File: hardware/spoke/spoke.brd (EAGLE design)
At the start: 53.3 x 37.8 mm, 22 parts, among them IC1 7805, J1 AVR_SPI_PRG_6PTH, J2 POWER_JACKPTH, U1 ATMEGA328P_PDIP, U2 AT25M01-SHM-B, U3 NRF24L01+

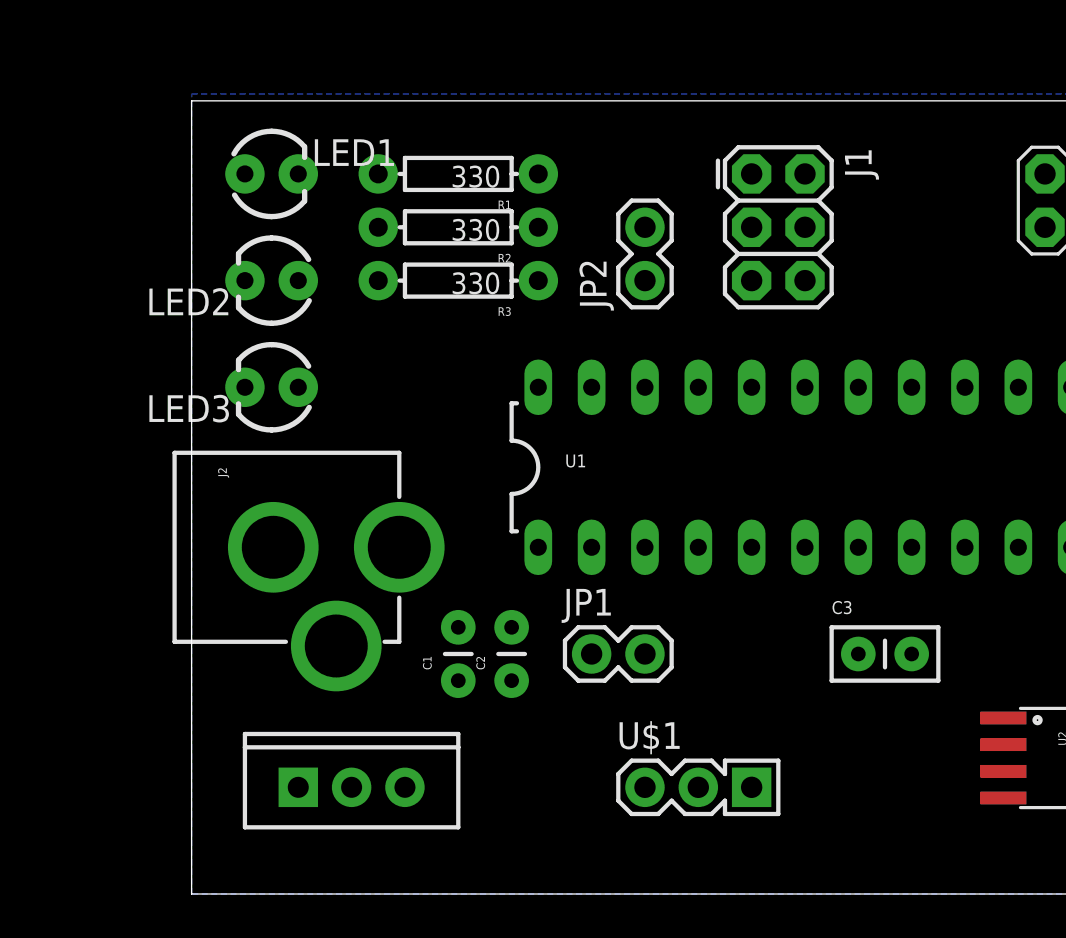
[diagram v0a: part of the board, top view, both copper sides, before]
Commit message: MOAR SMDs and 3.3v supply fixes
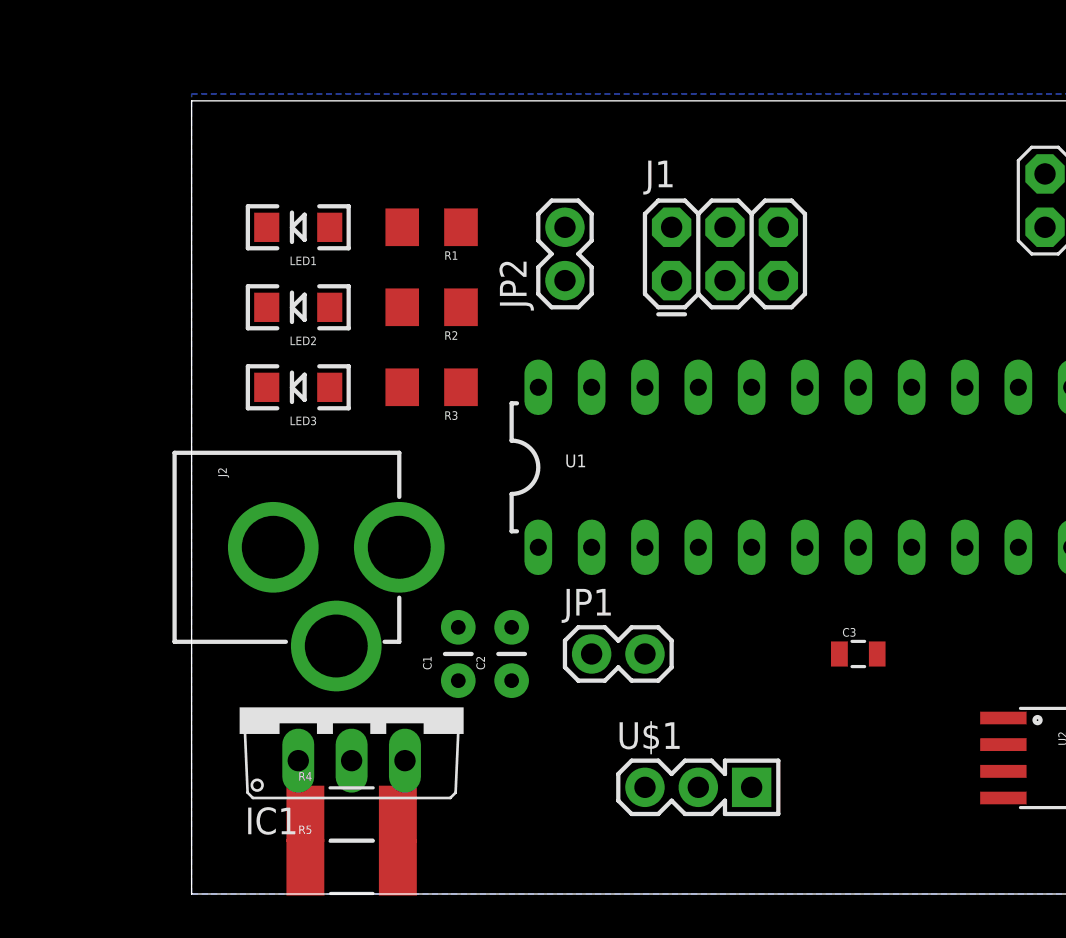
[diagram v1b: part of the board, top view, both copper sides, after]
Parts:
- added R4: 50, SparkFun-Passives:R2010
- added R5: 100, SparkFun-Passives:R2010
- C3: device SparkFun-Capacitors:CAP-PTH-SMALLEZ -> SparkFun-Passives:0805
- IC1: value 7805 -> 7805TV; device SparkFun-PowerIC:TO220-IGO -> linear:TO220V
- LED1, LED2, LED3: device SparkFun-LED:LED3MM -> SparkFun-LED:LED-1206
- R1, R2, R3: device SparkFun-Passives:AXIAL-0.3EZ -> SparkFun-Passives:1206
- moved J1 6.35 mm to (22.9, 29.2), turned to 0 degrees
- moved R3 5.24 mm to (11.4, 24.1)
- moved R2 4.02 mm to (11.4, 27.9)
- moved IC1 3.81 mm to (7.62, 8.89)
- moved JP2 3.81 mm to (17.8, 29.2)
- moved LED1 2.84 mm to (5.08, 31.8), turned to 180 degrees
- moved R1 2.84 mm to (11.4, 31.8)
- moved LED2 1.80 mm to (5.08, 27.9)
- moved LED3 1.27 mm to (5.08, 24.1)
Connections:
- removed net VCC: C2.1, C3.1, IC1.OUT, J1.2, U$1.1, U1.7, U2.8, U3.2
- new net 3.3V: R4.2, R5.1, U2.8
- new net 5V: C2.1, C3.1, IC1.3, J1.2, R4.1, U$1.1, U1.7, U3.2
- net GND: now also IC1.2, LED1.C, LED2.C, LED3.C, R5.2; no longer IC1.GND, LED1.K, LED2.K, LED3.K
- net N$10: now also R1.2; no longer R1.P$2
- net N$11: now also R3.2; no longer R3.P$2
- net N$12: now also R1.1; no longer R1.P$1
- net N$13: now also R3.1; no longer R3.P$1
- net N$14: now also IC1.1; no longer IC1.IN
- net N$8: now also R2.2; no longer R2.P$2
- net N$9: now also R2.1; no longer R2.P$1

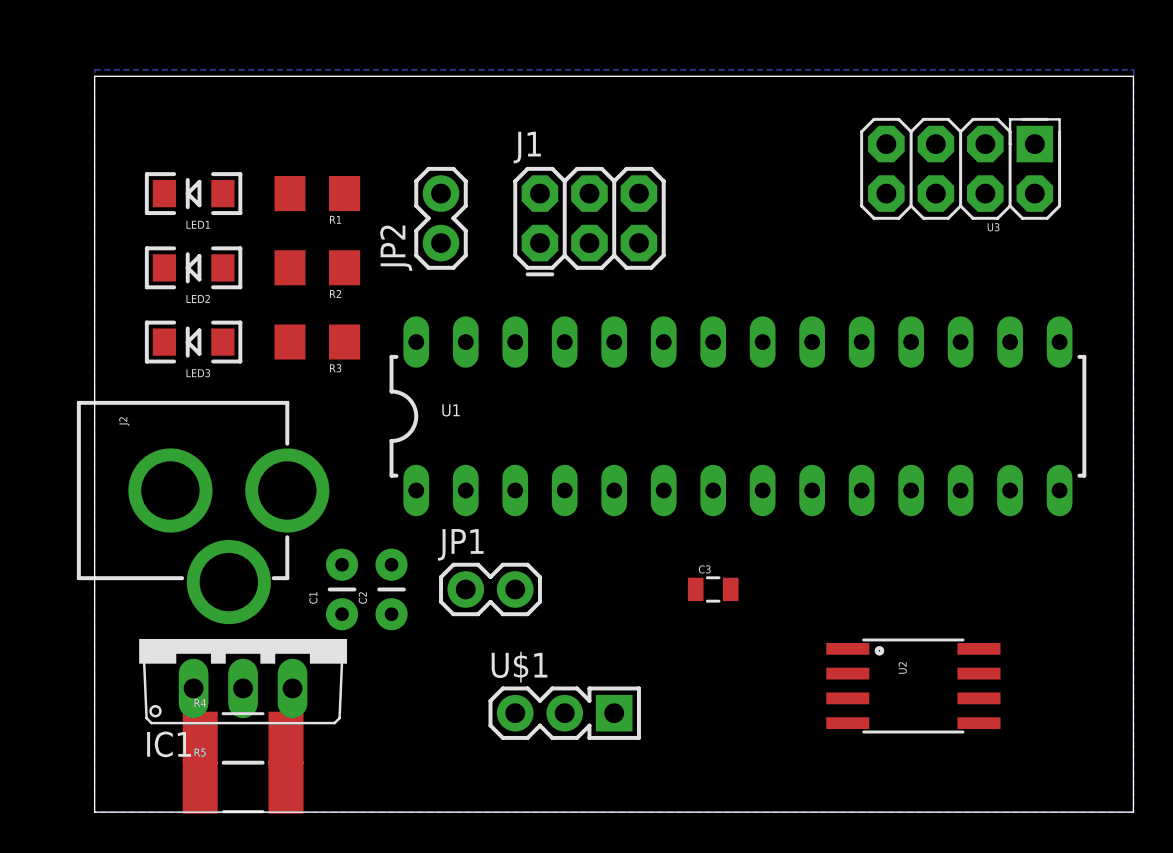
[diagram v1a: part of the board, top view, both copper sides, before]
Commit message: Update schematic from todos
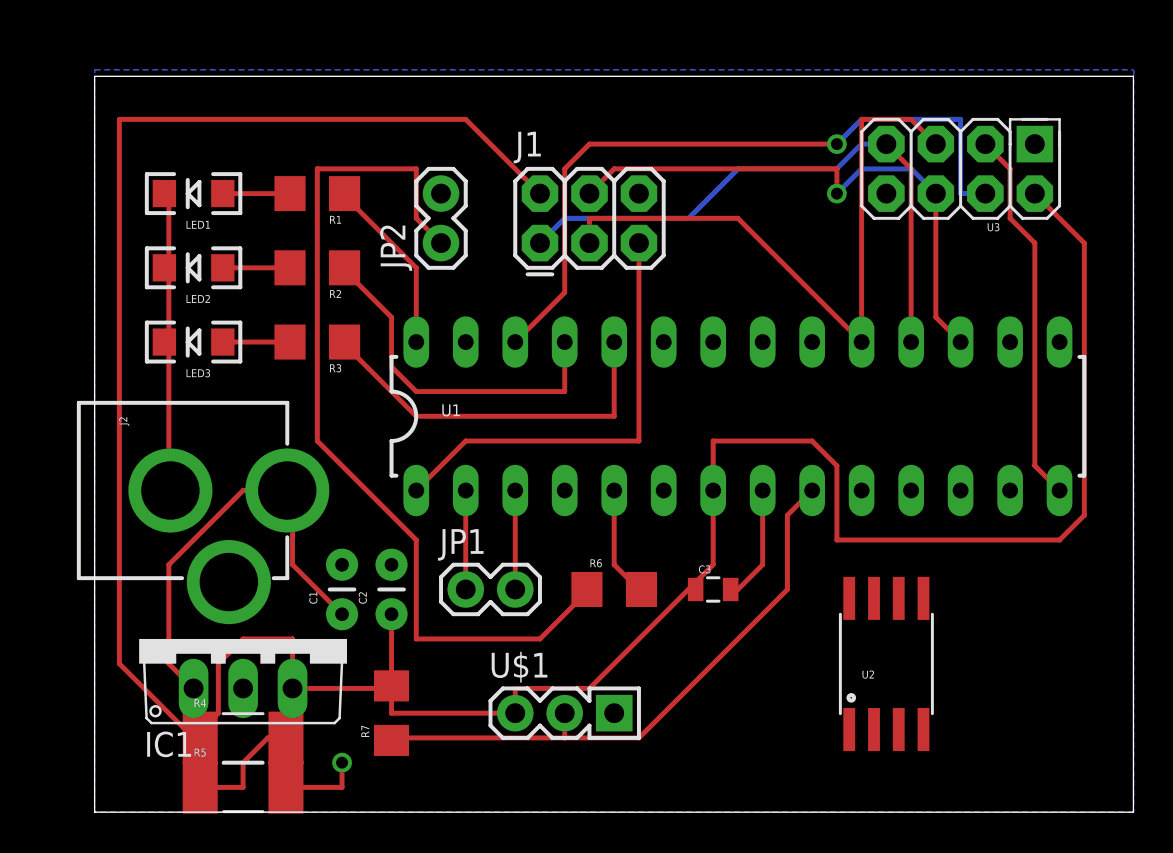
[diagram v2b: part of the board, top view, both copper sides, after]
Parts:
- added R6: 330, SparkFun-Passives:1206
- added R7: 5k, SparkFun-Passives:1206
- moved U2 1.81 mm to (40.6, 7.62), turned to 0 degrees
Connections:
- removed net N$6: U$1.2, U1.11
- new net N$15: JP2.1, R6.1
- new net N$16: R6.2, U1.5
- net 5V: now also R7.2
- net N$1: now also R7.1, U$1.2, U1.9; no longer JP2.1, U1.15
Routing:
- net 5V: track 0.00 -> 146.8 mm
- net N$15: track 0.00 -> 45.7 mm
- net N$5: track 0.00 -> 36.4 mm, vias 0 -> 1
- net SCK: track 0.00 -> 33.6 mm
- net MISO: track 0.00 -> 30.6 mm
- net N$1: track 0.00 -> 30.5 mm
- net MOSI: track 0.00 -> 28.8 mm, vias 0 -> 1
- net GND: track 0.00 -> 26.1 mm, vias 0 -> 1
- net RESET: track 0.00 -> 22.6 mm
- net N$14: track 0.00 -> 22.2 mm
- net N$13: track 0.00 -> 19.5 mm
- net N$7: track 0.00 -> 19.4 mm
- net N$9: track 0.00 -> 18.2 mm
- net N$12: track 0.00 -> 9.33 mm
- net 3.3V: track 0.00 -> 6.88 mm
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
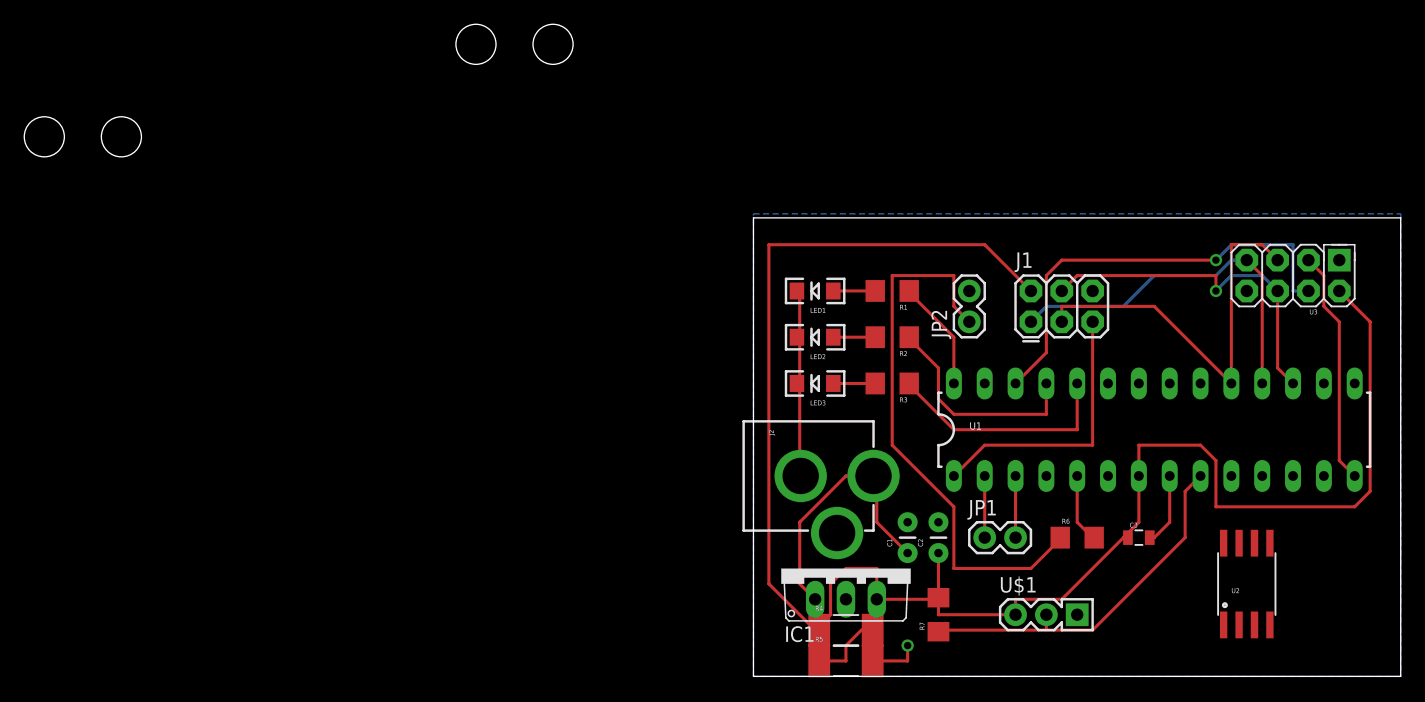
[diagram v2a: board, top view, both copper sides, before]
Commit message: Adjust schematic. Begin routing.
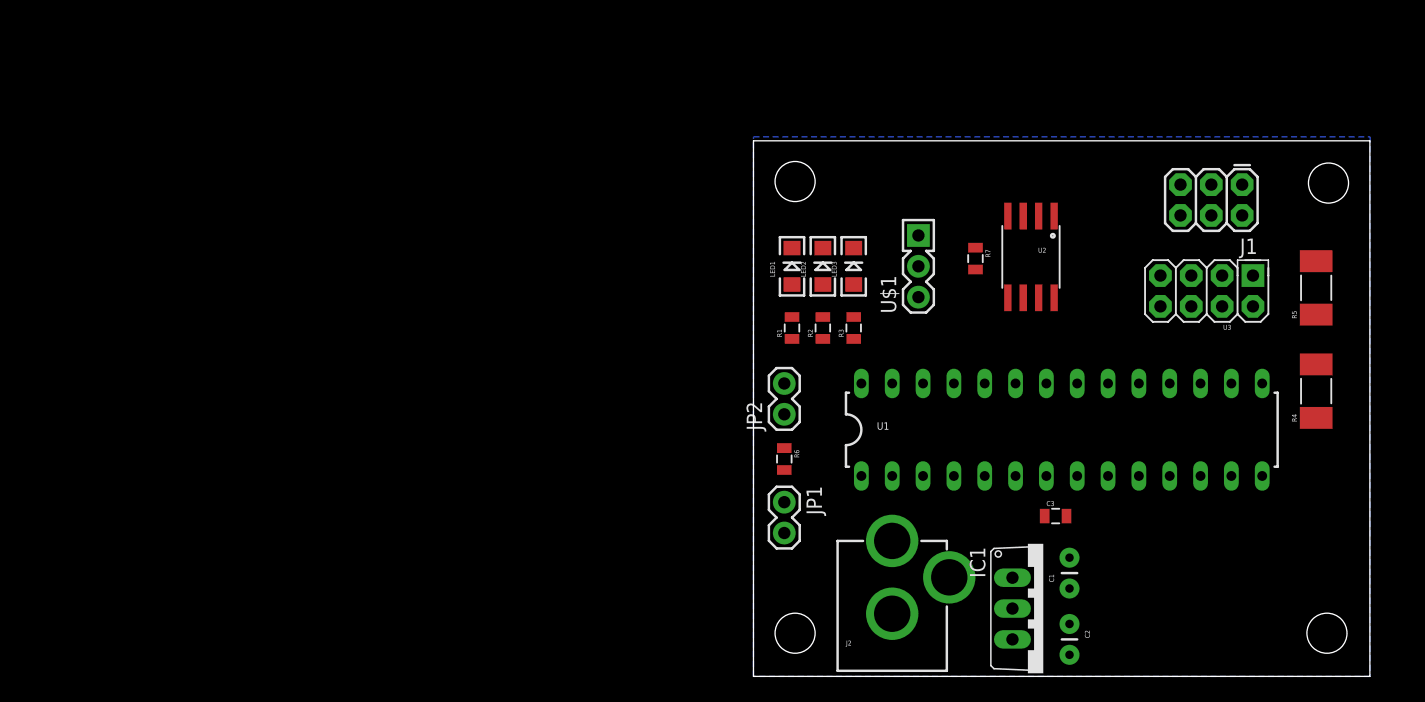
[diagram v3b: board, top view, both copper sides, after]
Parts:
- R1, R2, R3, R6, R7: device SparkFun-Passives:1206 -> SparkFun-Resistors:0805
- moved STANDOFF2 113.3 mm to (47.2, 3.56)
- moved STANDOFF4 71.2 mm to (47.4, 40.6)
- moved STANDOFF1 68.9 mm to (3.43, 3.56)
- moved R5 49.4 mm to (46.4, 32.0), turned to 90 degrees
- moved R4 43.4 mm to (46.4, 23.5), turned to 90 degrees
- moved U2 32.3 mm to (22.9, 34.5), turned to 180 degrees
- moved R7 29.5 mm to (18.3, 34.4), turned to 270 degrees
- moved U$1 27.4 mm to (13.6, 31.2), turned to 90 degrees
- moved R6 25.0 mm to (2.54, 17.9), turned to 270 degrees
- moved J2 24.4 mm to (11.4, -2.54), turned to 0 degrees
- moved STANDOFF3 22.9 mm to (3.43, 40.8)
- moved J1 20.7 mm to (40.3, 40.5), turned to 180 degrees
- moved JP2 17.0 mm to (2.54, 21.6)
- moved JP1 16.8 mm to (2.54, 14.4), turned to 270 degrees
- moved IC1 16.6 mm to (23.9, 5.59), turned to 270 degrees
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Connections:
- removed net N$13: R3.1, U1.24
- new net N$6: U1.15, U2.1
- net N$3: now also R2.1; no longer U2.1
- net N$5: now also R3.1; no longer U3.3
- net N$9: now also U1.16, U3.3; no longer R2.1, U1.25
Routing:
- net 5V: track 146.8 -> 0.00 mm
- net N$15: track 45.7 -> 0.00 mm
- net N$5: track 36.4 -> 0.00 mm, vias 1 -> 0
- net SCK: track 33.6 -> 0.00 mm
- net MISO: track 30.6 -> 0.00 mm
- net N$1: track 30.5 -> 0.00 mm
- net MOSI: track 28.8 -> 0.00 mm, vias 1 -> 0
- net GND: track 26.1 -> 0.00 mm, vias 1 -> 0
- net RESET: track 22.6 -> 0.00 mm
- net N$14: track 22.2 -> 0.00 mm
- net N$13: track 19.5 -> 0.00 mm
- net N$7: track 19.4 -> 0.00 mm
- net N$9: track 18.2 -> 0.00 mm
- net N$12: track 9.33 -> 0.00 mm
- net 3.3V: track 6.88 -> 0.00 mm
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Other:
- board size 53.3 x 37.8 mm -> 50.8 x 44.1 mm

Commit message: Finish routing spoke!
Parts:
- removed R4: 50, SparkFun-Passives:R2010
- removed R5: 100, SparkFun-Passives:R2010
- added 1000: 100, SparkFun-Resistors:0805
- added 500: 50, SparkFun-Resistors:0805
- added U$2: (no value), SparkFun-Aesthetics:OSHW-LOGO-S
- moved JP2 10.2 mm to (2.54, 11.4), turned to 270 degrees
- moved R7 6.07 mm to (12.6, 32.4)
- moved R6 3.79 mm to (3.43, 14.2), turned to 0 degrees
- moved U$1 2.54 mm to (16.1, 31.2)
- moved JP1 2.54 mm to (2.54, 16.9), turned to 90 degrees
- moved C3 0.13 mm to (25.0, 13.2)
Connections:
- removed net N$6: U1.15, U2.1
- new net DHT-IN: R7.1, U$1.2, U1.25
- net 3.3V: now also 1000.1, 500.2, U3.2; no longer R4.2, R5.1, U2.8
- net 5V: now also 500.1, U1.20, U2.8; no longer R4.1, U3.2
- net GND: now also 1000.2; no longer R5.2
- net N$1: now also U1.24, U2.1; no longer R7.1, U$1.2, U1.9
- net N$7: now also U1.15; no longer U1.14
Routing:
- net 5V: track 0.00 -> 129.6 mm, vias 0 -> 2
- net RESET: track 0.00 -> 61.3 mm
- net MISO: track 0.00 -> 53.0 mm
- net SCK: track 0.00 -> 50.2 mm, vias 0 -> 2
- net MOSI: track 0.00 -> 40.3 mm, vias 0 -> 2
- net N$7: track 0.00 -> 19.3 mm
- net N$1: track 0.00 -> 18.8 mm, vias 0 -> 1
- net N$14: track 0.00 -> 16.2 mm
- net DHT-IN: track 0.00 -> 16.0 mm
- net N$16: track 0.00 -> 15.7 mm
- net GND: track 0.00 -> 15.1 mm
- net N$4: track 0.00 -> 14.1 mm
- net N$2: track 0.00 -> 11.6 mm
- net 3.3V: track 0.00 -> 8.39 mm
- net N$3: track 0.00 -> 7.53 mm
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- added copper zone on layer 1, net GND
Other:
- board text added: "0.1uf"
- board text added: "0.33uf"
- board text added: "1000"
- board text added: "22pf"
- board text added: "330"
- board text added: "500"
- board text added: "5k"
- board text added: "ATMEGA328P"
- board text added: "DHT11"
- board text added: "G"
- board text added: "ICSP"
- board text added: "IR_LED"
- board text added: "NRF24L01+"
- board text added: "R"
- board text added: "RXD"
- board text added: "TXD"
- board text added: "Y"
- board text added: "aurai - spoke rev 1"
- board text added: "thomas rix"
- board text added: "trix.io"

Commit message: Update spoke board
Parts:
- removed 1000: 100, SparkFun-Resistors:0805
- removed 500: 50, SparkFun-Resistors:0805
- removed R2, R3, R6: 330, SparkFun-Resistors:0805
- removed U$2: (no value), SparkFun-Aesthetics:OSHW-LOGO-S
- removed U2: AT25M01-SHM-B, aurai:SO08-EIAJ
- added C4, C5: 0.1uF, SparkFun-Capacitors:0805
- added IC2: LM3490, aurai:SOT23-5
- C1, C2: device SparkFun-Capacitors:CAP-PTH-SMALL -> SparkFun-Capacitors:0805
- R1: device SparkFun-Resistors:0805 -> aurai:CRA06S08
- moved J1 17.4 mm to (23.2, 37.0), turned to 0 degrees
- moved JP2 5.73 mm to (2.16, 17.1)
- moved JP1 5.60 mm to (2.16, 11.3), turned to 270 degrees
- moved STANDOFF4 5.08 mm to (42.3, 40.6)
- moved STANDOFF2 5.08 mm to (42.2, 3.56)
- moved LED1 1.27 mm to (4.45, 33.8)
- moved LED2 1.27 mm to (6.99, 33.8)
- moved C2 1.27 mm to (26.0, 3.05)
- moved LED3 1.27 mm to (9.53, 33.8)
- moved R1 0.99 mm to (3.81, 27.9), turned to 180 degrees
- moved C1 0.13 mm to (25.9, 7.24), turned to 270 degrees
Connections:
- removed net N$10: LED1.A, R1.2
- removed net N$11: LED3.A, R3.2
- new net N$6: LED3.A, R1.1
- net 3.3V: now also C5.1, IC2.5; no longer 1000.1, 500.2
- net 5V: now also C4.1, IC2.3, IC2.4; no longer 500.1, U2.8
- net GND: now also C4.2, C5.2, IC2.2; no longer 1000.2, U2.4
- net MISO: no longer U2.2
- net MOSI: no longer U2.5
- net N$1: now also LED1.A, R1.3; no longer U1.24, U2.1
- net N$12: now also R1.6; no longer R1.1
- net N$15: now also R1.4; no longer R6.1
- net N$16: now also R1.5; no longer R6.2
- net N$3: now also R1.7; no longer R2.1
- net N$5: now also R1.8; no longer R3.1
- net N$8: now also R1.2; no longer R2.2
- net SCK: no longer U2.6
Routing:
- net 5V: track 129.6 -> 78.1 mm, vias 2 -> 0
- net MISO: track 53.0 -> 22.6 mm
- net 3.3V: track 8.39 -> 32.2 mm
- net SCK: track 50.2 -> 28.8 mm, vias 2 -> 1
- net N$1: track 18.8 -> 3.79 mm, vias 1 -> 0
- net N$15: track 2.80 -> 13.0 mm
- net GND: track 15.1 -> 5.38 mm
- net N$16: track 15.7 -> 22.5 mm
- net N$6: track 0.00 -> 6.71 mm
- net N$2: track 11.6 -> 17.9 mm
- net MOSI: track 40.3 -> 34.3 mm, vias 2 -> 1
- net N$5: track 7.24 -> 10.8 mm
- net N$3: track 7.53 -> 10.9 mm
- net RESET: track 61.3 -> 58.4 mm
- net N$11: track 2.68 -> 0.00 mm
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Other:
- board size 50.8 x 44.1 mm -> 45.7 x 44.1 mm
- board text removed: "1000"
- board text removed: "500"
